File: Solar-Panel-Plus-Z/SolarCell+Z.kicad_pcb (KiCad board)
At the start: 6 copper layers, 48.4 x 48.4 mm, 63 parts, among them J1 XF2M-1015-1A, U2 Value, U3 Value

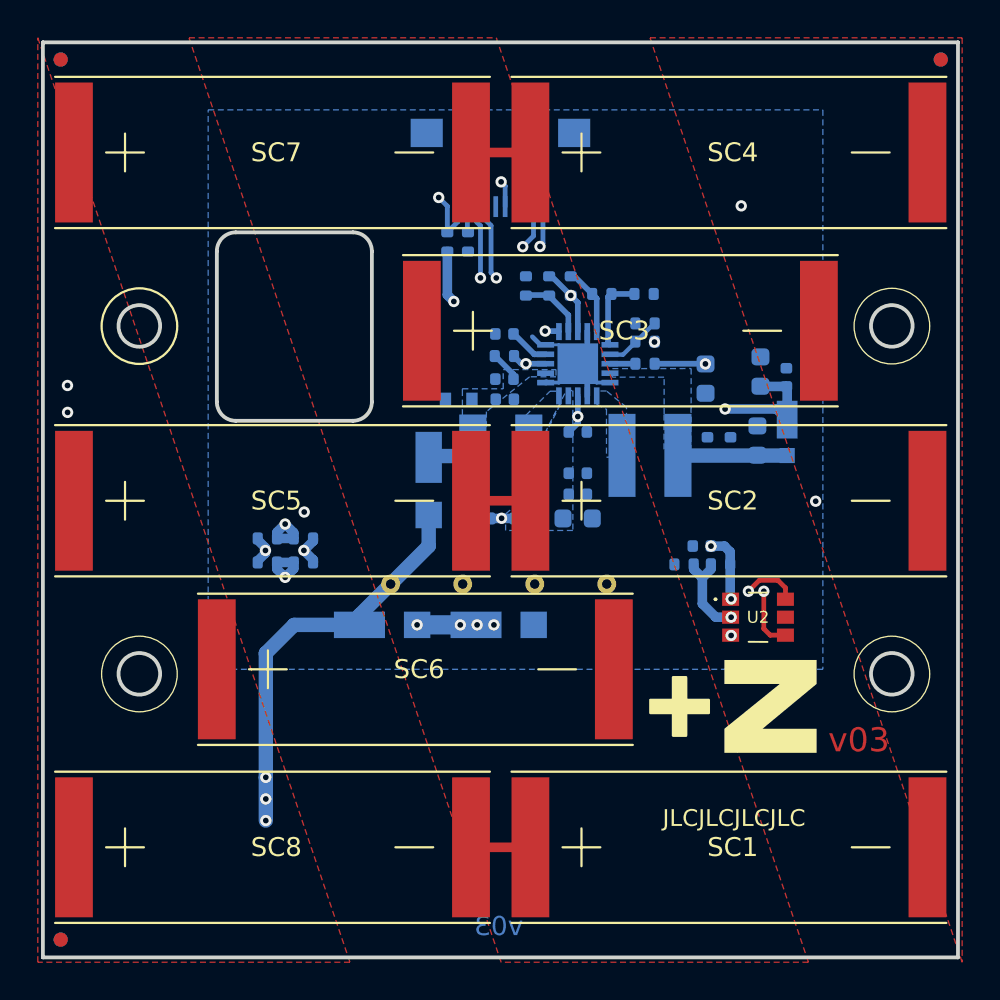
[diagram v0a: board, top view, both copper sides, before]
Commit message: Done with X, +/-Y, and +Z. TODO: -Z
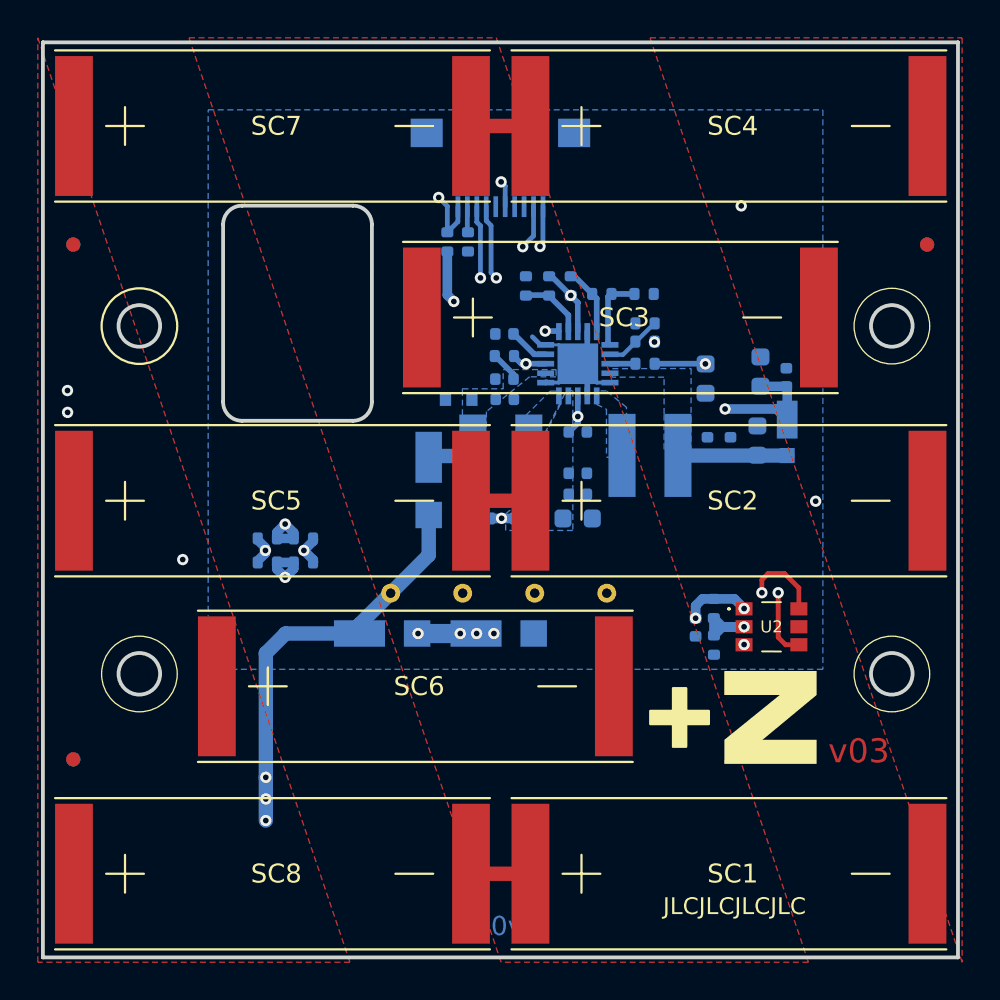
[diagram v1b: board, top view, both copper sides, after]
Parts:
- moved REF** 9.81 mm to (175.1, 83.3) (x2)
- moved REF** 9.81 mm to (129.9, 83.3) (x2)
- moved REF** 9.56 mm to (129.9, 110.5) (x2)
- moved R2 4.55 mm to (163.8, 104.4), turned to 90 degrees
- moved C1 4.31 mm to (162.8, 103.5), turned to 90 degrees
- moved R1 2.37 mm to (163.8, 102.5), turned to 90 degrees
- moved SC4 1.40 mm to (154.1, 77.0)
- moved SC1 1.40 mm to (154.1, 116.5)
- moved SC7 1.40 mm to (129.9, 77.0)
- moved SC8 1.40 mm to (129.9, 116.5)
- moved SC6 0.90 mm to (137.5, 106.6)
- moved U2 0.87 mm to (166.8, 103.5)
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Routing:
- net /coil: track 15619.4 -> 13159.2 mm
- net +3V3: track 45.9 -> 49.8 mm
- net SDA1: track 29.3 -> 30.9 mm
- net SCL1: track 29.7 -> 30.4 mm
- net Net-(R1-Pad1): track 5.00 -> 4.48 mm
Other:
- outline, holes or cut-outs redrawn
